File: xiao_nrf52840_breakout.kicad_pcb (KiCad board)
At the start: 2 copper layers, 17.8 x 35.7 mm, 12 parts, among them J1 53261-0271, J10 Conn_01x01, J2 Conn_01x07, J3 Conn_01x07, J4 Conn_01x01, J5 Conn_01x03, J6 Conn_02x02_Odd_Even, J7 Conn_01x03, J8 Conn_01x01, J9 Conn_01x01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

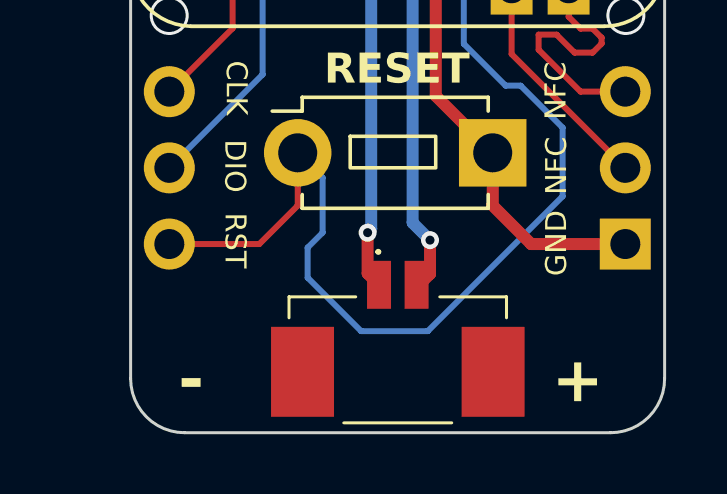
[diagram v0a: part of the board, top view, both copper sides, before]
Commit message: add extra bat+ and bat- pins
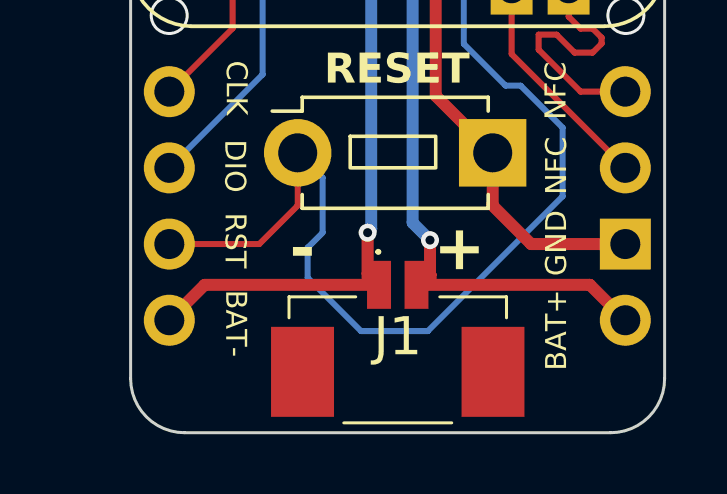
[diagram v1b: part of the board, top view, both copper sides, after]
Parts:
- J5, J7: value Conn_01x03 -> Conn_01x04; footprint Connector_PinSocket_2.54mm:PinSocket_1x03_P2.54mm_Vertical -> Connector_PinSocket_2.54mm:PinSocket_1x04_P2.54mm_Vertical
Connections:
- J1 pad 1: Net-(J9-Pin_1) -> BAT-
- J1 pad 2: Net-(J10-Pin_1) -> BAT+
- J10 pad 1: Net-(J10-Pin_1) -> BAT+
- J9 pad 1: Net-(J9-Pin_1) -> BAT-
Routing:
- net BAT-: track 0.00 -> 32.6 mm, vias 0 -> 2
- net BAT+: track 0.00 -> 31.7 mm, vias 0 -> 2
- net Net-(J9-Pin_1): track 25.1 -> 0.00 mm, vias 2 -> 0
- net Net-(J10-Pin_1): track 24.3 -> 0.00 mm, vias 2 -> 0
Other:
- board text added: "BAT+"
- board text added: "BAT-"
